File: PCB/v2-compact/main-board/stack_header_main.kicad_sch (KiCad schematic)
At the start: 0 parts

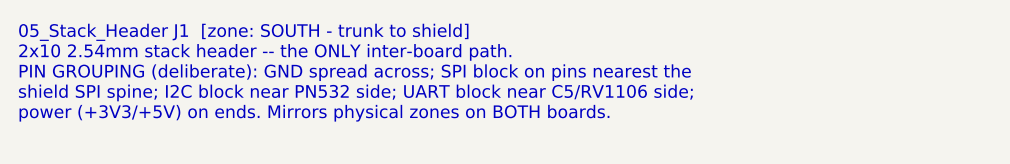
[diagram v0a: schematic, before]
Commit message: PCB: rework main board to phone-style layout; J1 -> horizontal strip
Main board (per feedback) is now a phone-style split — front is pure UI, back
carries the electronics:
- FRONT: status LEDs at the very top (above the display), TFT rotated to
  LANDSCAPE (sideways), nav buttons below it and moved down. Same feel as the
  ESP32-DIV, sideways screen.
- BACK: ESP32-S3 behind the display, microSD beside it, power + USB-C at the
  bottom-centre edge like a phone.

To keep the centre column free for the landscape display and the bottom-centre
USB-C, J1 is reoriented from a vertical 2x10 to a HORIZONTAL 10x2 strip in the
lower-centre. J1 is the shared mating datum, so the shield's J1 moves to match;
the shield's RV1106 / HTRC110 / bulk-cap zones shift to sit above/below the new
strip (SPI spine still runs north from it). Every v1 capability unchanged.

Updated both .kicad_pcb, both floorplan SVGs, both schematics' zone specs, and
PLACEMENT.md. Verified: files parse, J1 clears all zones, no same-side overlaps.

Co-Authored-By: Claude <noreply@anthropic.com>
Claude-Session: https://claude.ai/code/session_017BEAKBRVwbUCc7Sa2o3Ye7
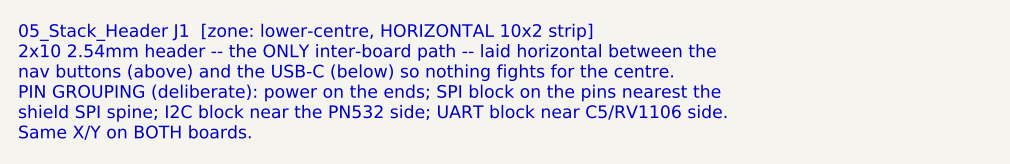
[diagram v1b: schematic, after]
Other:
- note added: "05_Stack_Header J1 [zone: lower-centre, HORIZONTAL 10x2 strip] 2x10 2.54mm header -- the ONLY inter-board path -- laid horizontal between the nav buttons (above) and the USB-C (below) so nothing fights for the centre. PIN GROUPING (deliberate): power on the ends; SPI block on the pins nearest the shield SPI spine; I2C block near the PN532 side; UART block near C5/RV1106 side. Same X/Y on BOTH boa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"
- note removed: "05_Stack_Header J1 [zone: SOUTH - trunk to shield] 2x10 2.54mm stack header -- the ONLY inter-board path. PIN GROUPING (deliberate): GND spread across; SPI block on pins nearest the shield SPI spine; I2C block near PN532 side; UART block near C5/RV1106 side; power (+3V3/+5V) on ends. Mirrors physical zones on BOTH boards."
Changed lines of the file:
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@@
   (paper "A4")
   (title_block (title "05_Stack_Header") (company "YurilLAB"))
-  (text "05_Stack_Header J1  [zone: SOUTH - trunk to shield]
-2x10 2.54mm stack header -- the ONLY inter-board path.
-PIN GROUPING (deliberate): GND spread across; SPI block on pins nearest the
-shield SPI spine; I2C block near PN532 side; UART block near C5/RV1106 side;
-power (+3V3/+5V) on ends. Mirrors physical zones on BOTH boards." (at 15 15 0)
+  (text "05_Stack_Header J1  [zone: lower-centre, HORIZONTAL 10x2 strip]
+2x10 2.54mm header -- the ONLY inter-board path -- laid horizontal between the
+nav buttons (above) and the USB-C (below) so nothing fights for the centre.
+PIN GROUPING (deliberate): power on the ends; SPI block on the pins nearest the
+shield SPI spine; I2C block near the PN532 side; UART block near C5/RV1106 side.
+Same X/Y on BOTH boards." (at 15 15 0)
     (effects (font (size 1.4 1.4)) (justify left top)))
   (sheet_instances (path "/" (page "1")))
